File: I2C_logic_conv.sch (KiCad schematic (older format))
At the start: 8 parts, among them U4 PCA9306

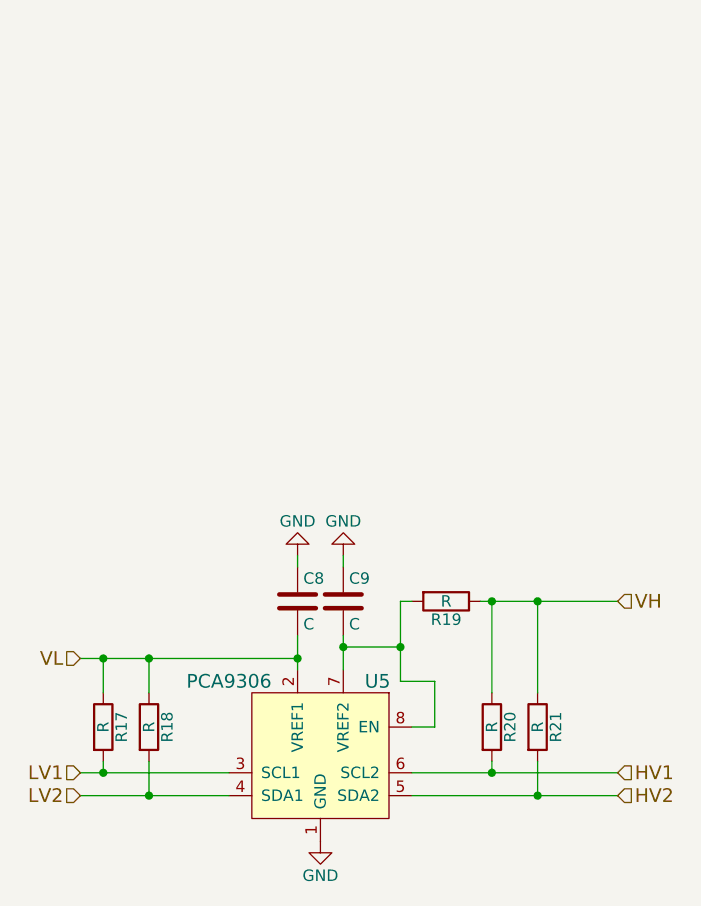
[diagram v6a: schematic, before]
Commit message: 部品に定数を追加
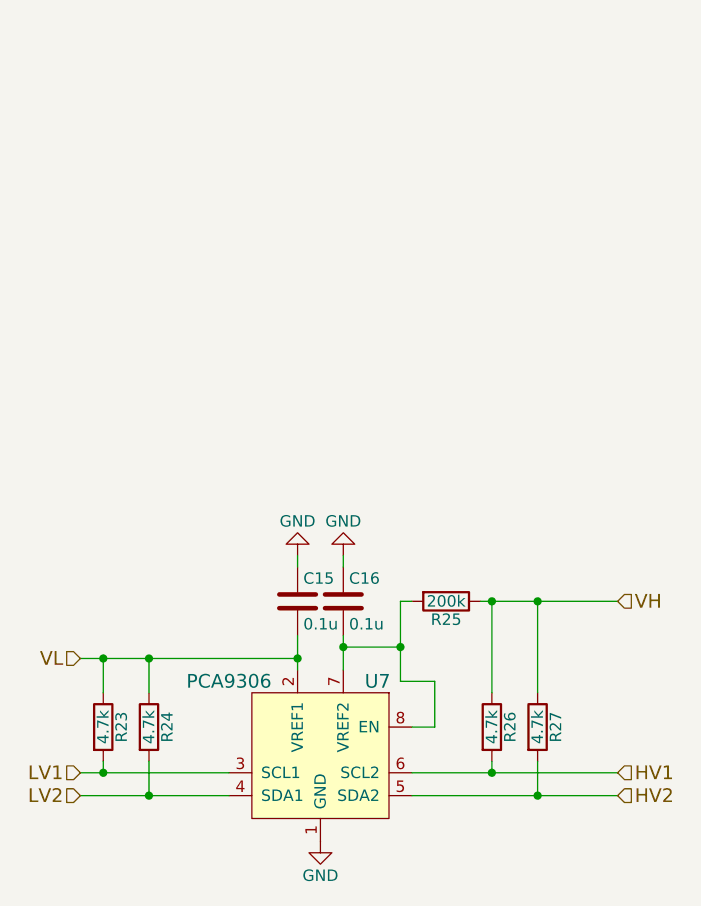
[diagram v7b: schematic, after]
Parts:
- C6, C7: value C -> 0.1u
- R12, R13, R15, R16: value R -> 4.7k
- R14: value R -> 200k
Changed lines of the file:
@@
 Date "2016-12-18"
 Rev "1.1"
-Comp "Manju-Honpo"
+Comp "Manju-Hompo"
 Comment1 "@C91"
 Comment2 "Designed by @yuqlid"
@@
 AR Path="/583898DE/5838B993" Ref="R17"  Part="1"
 AR Path="/583E5F3D/5838B993" Ref="R23"  Part="1"
-F 0 "R17" V 5030 4150 50  0000 C CNN
-F 1 "R" V 4950 4150 50  0000 C CNN
+F 0 "R23" V 5030 4150 50  0000 C CNN
+F 1 "4.7k" V 4950 4150 50  0000 C CNN
 F 2 "Resistors_SMD:R_0603" V 4880 4150 50  0001 C CNN
 F 3 "" H 4950 4150 50  0000 C CNN
@@
 AR Path="/583898DE/5838BA42" Ref="R18"  Part="1"
 AR Path="/583E5F3D/5838BA42" Ref="R24"  Part="1"
-F 0 "R18" V 5230 4150 50  0000 C CNN
-F 1 "R" V 5150 4150 50  0000 C CNN
+F 0 "R24" V 5230 4150 50  0000 C CNN
+F 1 "4.7k" V 5150 4150 50  0000 C CNN
 F 2 "Resistors_SMD:R_0603" V 5080 4150 50  0001 C CNN
 F 3 "" H 5150 4150 50  0000 C CNN
@@
 AR Path="/583898DE/5838BBE6" Ref="R20"  Part="1"
 AR Path="/583E5F3D/5838BBE6" Ref="R26"  Part="1"
-F 0 "R20" V 6730 4150 50  0000 C CNN
-F 1 "R" V 6650 4150 50  0000 C CNN
+F 0 "R26" V 6730 4150 50  0000 C CNN
+F 1 "4.7k" V 6650 4150 50  0000 C CNN
 F 2 "Resistors_SMD:R_0603" V 6580 4150 50  0001 C CNN
 F 3 "" H 6650 4150 50  0000 C CNN
@@
 AR Path="/583898DE/5838BC03" Ref="R21"  Part="1"
 AR Path="/583E5F3D/5838BC03" Ref="R27"  Part="1"
-F 0 "R21" V 6930 4150 50  0000 C CNN
-F 1 "R" V 6850 4150 50  0000 C CNN
+F 0 "R27" V 6930 4150 50  0000 C CNN
+F 1 "4.7k" V 6850 4150 50  0000 C CNN
 F 2 "Resistors_SMD:R_0603" V 6780 4150 50  0001 C CNN
 F 3 "" H 6850 4150 50  0000 C CNN
@@
 AR Path="/583898DE/583C3211" Ref="U5"  Part="1"
 AR Path="/583E5F3D/583C3211" Ref="U7"  Part="1"
-F 0 "U5" H 6150 4750 60  0000 C CNN
+F 0 "U7" H 6150 4750 60  0000 C CNN
 F 1 "PCA9306" H 5500 4750 60  0000 C CNN
 F 2 "Housings_SSOP:MSOP-8_3x3mm_Pitch0.65mm" H 5800 4350 60  0001 C CNN
@@
 AR Path="/583898DE/583C3B42" Ref="#PWR090"  Part="1"
 AR Path="/583E5F3D/583C3B42" Ref="#PWR0101"  Part="1"
-F 0 "#PWR090" H 5900 4400 50  0001 C CNN
+F 0 "#PWR0101" H 5900 4400 50  0001 C CNN
 F 1 "GND" H 5900 4500 50  0000 C CNN
 F 2 "" H 5900 4650 50  0000 C CNN
@@
 AR Path="/583898DE/583C3E21" Ref="C8"  Part="1"
 AR Path="/583E5F3D/583C3E21" Ref="C15"  Part="1"
-F 0 "C8" H 5825 3700 50  0000 L CNN
-F 1 "C" H 5825 3500 50  0000 L CNN
+F 0 "C15" H 5825 3700 50  0000 L CNN
+F 1 "0.1u" H 5825 3500 50  0000 L CNN
 F 2 "Capacitors_SMD:C_0603" H 5838 3450 50  0001 C CNN
 F 3 "" H 5800 3600 50  0000 C CNN
@@
 AR Path="/583898DE/583C3EB8" Ref="C9"  Part="1"
 AR Path="/583E5F3D/583C3EB8" Ref="C16"  Part="1"
-F 0 "C9" H 6025 3700 50  0000 L CNN
-F 1 "C" H 6025 3500 50  0000 L CNN
+F 0 "C16" H 6025 3700 50  0000 L CNN
+F 1 "0.1u" H 6025 3500 50  0000 L CNN
 F 2 "Capacitors_SMD:C_0603" H 6038 3450 50  0001 C CNN
 F 3 "" H 6000 3600 50  0000 C CNN
@@
 AR Path="/583898DE/583C3F2C" Ref="#PWR091"  Part="1"
 AR Path="/583E5F3D/583C3F2C" Ref="#PWR0102"  Part="1"
-F 0 "#PWR091" H 5800 3150 50  0001 C CNN
+F 0 "#PWR0102" H 5800 3150 50  0001 C CNN
 F 1 "GND" H 5800 3250 50  0000 C CNN
 F 2 "" H 5800 3400 50  0000 C CNN
@@
 AR Path="/583898DE/583C4151" Ref="#PWR092"  Part="1"
 AR Path="/583E5F3D/583C4151" Ref="#PWR0103"  Part="1"
-F 0 "#PWR092" H 6000 3150 50  0001 C CNN
+F 0 "#PWR0103" H 6000 3150 50  0001 C CNN
 F 1 "GND" H 6000 3250 50  0000 C CNN
 F 2 "" H 6000 3400 50  0000 C CNN
@@
 AR Path="/583898DE/583C426E" Ref="R19"  Part="1"
 AR Path="/583E5F3D/583C426E" Ref="R25"  Part="1"
-F 0 "R19" V 6530 3600 50  0000 C CNN
-F 1 "R" V 6450 3600 50  0000 C CNN
+F 0 "R25" V 6530 3600 50  0000 C CNN
+F 1 "200k" V 6450 3600 50  0000 C CNN
 F 2 "Resistors_SMD:R_0603" V 6380 3600 50  0001 C CNN
 F 3 "" H 6450 3600 50  0000 C CNN
